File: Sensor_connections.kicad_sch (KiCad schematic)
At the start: 0 parts

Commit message: Update Sensor_connections.kicad_sch
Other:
- note added: "Flex fuel sensor is not used in current configuration. Connected to breakout connector for future developments The EGO_Sensor is connected to a lambda sensor (located in the exhaust system). The lambda sensor is also connected to the battery +12V through a 5-Amp fuse (for pre-heating the sensor to operating temperature)."
- note removed: "rFlex fuel sensor is not used in current configuration. Connected to breakout connector for future developments The EGO_Sensor is connected to a lambda sensor (located in the exhaust system). The lambda sensor is also connected to the battery +12V through a 5-Amp fuse (for pre-heating the sensor to operating temperature)."
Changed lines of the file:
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@@
     (effects (font (size 1.6 1.6) (thickness 0.4) bold) (justify left bottom))
   )
-  (text "rFlex fuel sensor is not used in current configuration.\nConnected to breakout connector for future developments\n\nThe EGO_Sensor is connected to a lambda sensor (located in the \nexhaust system). The lambda sensor is also connected to the battery +12V through a \n5-Amp fuse (for pre-heating the sensor to operating temperature)."
+  (text "Flex fuel sensor is not used in current configuration.\nConnected to breakout connector for future developments\n\nThe EGO_Sensor is connected to a lambda sensor (located in the \nexhaust system). The lambda sensor is also connected to the battery +12V through a \n5-Amp fuse (for pre-heating the sensor to operating temperature)."
     (at 176.53 38.1 0)
     (effects (font (size 1.27 1.27)) (justify left bottom))

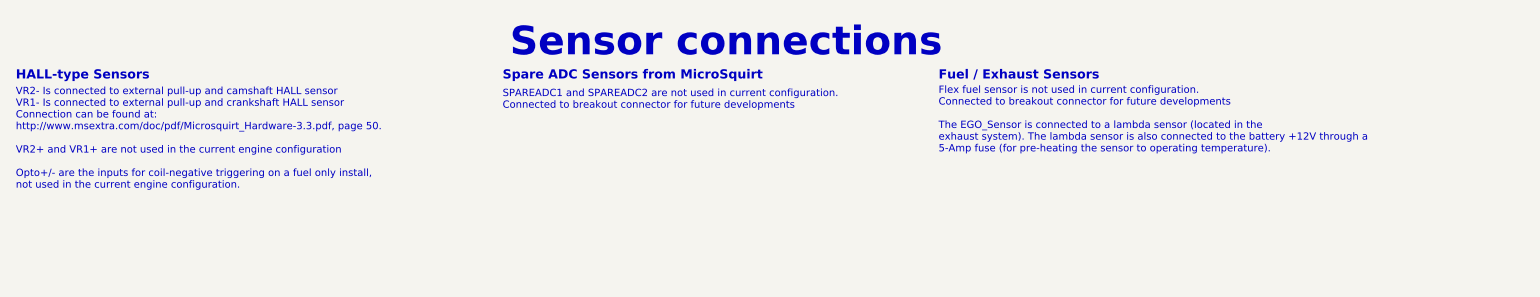
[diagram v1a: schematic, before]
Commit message: Added relays
Added relays to the schematic and noted that a relay for the fuel injectors is not needed.
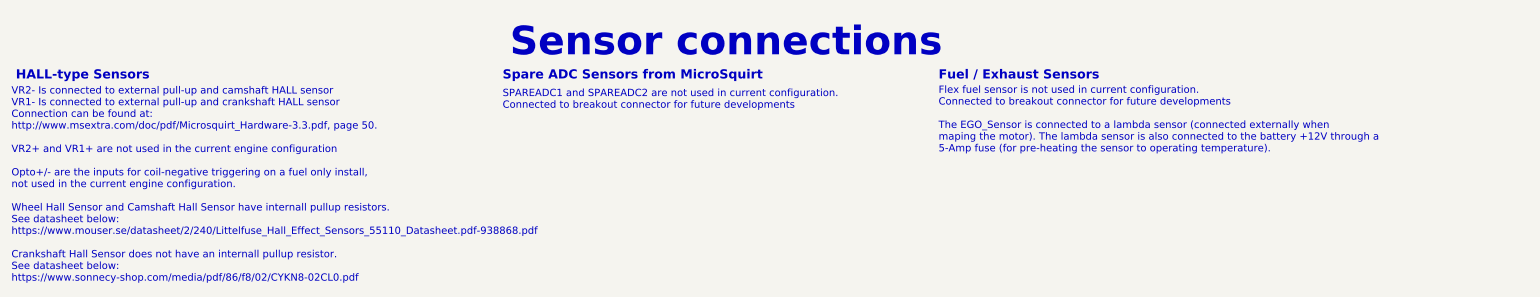
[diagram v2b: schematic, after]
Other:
- note added: "Flex fuel sensor is not used in current configuration. Connected to breakout connector for future developments The EGO_Sensor is connected to a lambda sensor (connected externally when maping the motor). The lambda sensor is also connected to the battery +12V through a 5-Amp fuse (for pre-heating the sensor to operating temperature)."
- note removed: "Flex fuel sensor is not used in current configuration. Connected to breakout connector for future developments The EGO_Sensor is connected to a lambda sensor (located in the exhaust system). The lambda sensor is also connected to the battery +12V through a 5-Amp fuse (for pre-heating the sensor to operating temperature)."
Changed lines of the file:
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@@
     (effects (font (size 5 5) (thickness 0.5) bold) (justify left bottom))
   )
-  (text "VR2- Is connected to external pull-up and camshaft HALL sensor\nVR1- Is connected to external pull-up and crankshaft HALL sensor\nConnection can be found at: \nhttp://www.msextra.com/doc/pdf/Microsquirt_Hardware-3.3.pdf, page 50.\n\nVR2+ and VR1+ are not used in the current engine configuration\n\nOpto+/- are the inputs for coil-negative triggering on a fuel only install,\nnot used in the current engine configuration."
-    (at 15.24 44.45 0)
+  (text "VR2- Is connected to external pull-up and camshaft HALL sensor\nVR1- Is connected to external pull-up and crankshaft HALL sensor\nConnection can be found at: \nhttp://www.msextra.com/doc/pdf/Microsquirt_Hardware-3.3.pdf, page 50.\n\nVR2+ and VR1+ are not used in the current engine configuration\n\nOpto+/- are the inputs for coil-negative triggering on a fuel only install,\nnot used in the current engine configuration.\n\nWheel Hall Sensor and Camshaft Hall Sensor have internall pullup resistors.\nSee datasheet below:\nhttps://www.mouser.se/datasheet/2/240/Littelfuse_Hall_Effect_Sensors_55110_Datasheet.pdf-938868.pdf\n\nCrankshaft Hall Sensor does not have an internall pullup resistor.\nSee datasheet below:\nhttps://www.sonnecy-shop.com/media/pdf/86/f8/02/CYKN8-02CL0.pdf\n"
+    (at 14.478 60.706 0)
     (effects (font (size 1.27 1.27)) (justify left bottom))
   )
@@
     (effects (font (size 1.6 1.6) (thickness 0.4) bold) (justify left bottom))
   )
-  (text "Flex fuel sensor is not used in current configuration.\nConnected to breakout connector for future developments\n\nThe EGO_Sensor is connected to a lambda sensor (located in the \nexhaust system). The lambda sensor is also connected to the battery +12V through a \n5-Amp fuse (for pre-heating the sensor to operating temperature)."
+  (text "Flex fuel sensor is not used in current configuration.\nConnected to breakout connector for future developments\n\nThe EGO_Sensor is connected to a lambda sensor (connected externally when \nmaping the motor). The lambda sensor is also connected to the battery +12V through a \n5-Amp fuse (for pre-heating the sensor to operating temperature)."
     (at 176.53 38.1 0)
     (effects (font (size 1.27 1.27)) (justify left bottom))
